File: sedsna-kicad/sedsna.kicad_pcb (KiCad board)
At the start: 2 copper layers, 8.8 x 9.5 mm, 47 parts, among them J1 Conn_01x03, J10 Conn_01x03, J2 Conn_01x03, J3 Servos_Rudder/Elevator, J4 L_Aileron, J5 USB4105-GF-A, J6 R_Aileron, J7 Prop, J8 Antenna, J9 Conn_01x03, U2 ESP32-C3, U4 Magnetometer, U5 IMU, U6 LDL1117S33R

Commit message: pcb layout started
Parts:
- removed BAT1: Conn_01x02, sedsna:CONN_SDA_42002-xxxxx_02_MOL
- removed BR1: Z4DGP406L-HF, TR3_V1:Z4DGP406L-HF_footprint_N
- removed J8: Antenna, sedsna:CONN_142-0701-801
- added AE1: Antenna, TR3_V1:GRADCONN_RFPC-SMA28-F, F.Cu at (125.2, 48.2)
- added J11: BAT1, sedsna:SHDR3W166P0X635_1X3_2032X762X1397P, F.Cu at (122.8, 84.5)
- C15, C17, C18, C23, C24, C3, C4, C5, C6, C7, FB1, R12, R16, R17, R18, R19, R2, R7, R8: moved to B.Cu
- J4, J6, J7: footprint sedsna:CONN_SDA_42002-xxxxx_03_MOL -> sedsna:SHDR3W166P0X635_1X3_2032X762X1397P
- moved L1 123.0 mm to (109.1, 55.2)
- moved U2 122.7 mm to (125.7, 56.6), turned to -45 degrees
- moved C9 122.1 mm to (108.7, 58.5)
- moved C8 122.0 mm to (109.0, 57.0)
- moved XTAL1 114.7 mm to (118.6, 57.0)
- moved B1 113.1 mm to (109.8, 61.0)
- moved C1 111.5 mm to (116.3, 59.7)
- moved C2 111.5 mm to (116.3, 61.7)
- moved C7 108.9 mm to (106.4, 68.2), turned to 180 degrees
- moved C3 108.5 mm to (122.8, 63.8), turned to 180 degrees
- moved U5 106.7 mm to (113.2, 65.8)
- moved FB1 105.3 mm to (122.8, 66.0), turned to 180 degrees
- moved C15 99.9 mm to (113.2, 72.5), turned to 180 degrees
- moved C6 94.3 mm to (105.5, 75.5), turned to 180 degrees
- moved U4 92.8 mm to (106.0, 68.2), turned to 90 degrees
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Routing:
- added copper zone on In2.Cu, net +3.3V
- added copper zone on B.Cu, net Earth
- added copper zone on F.Cu, net Earth
- added copper zone on In1.Cu, net Earth
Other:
- board outline removed
- copper layers 2 -> 4

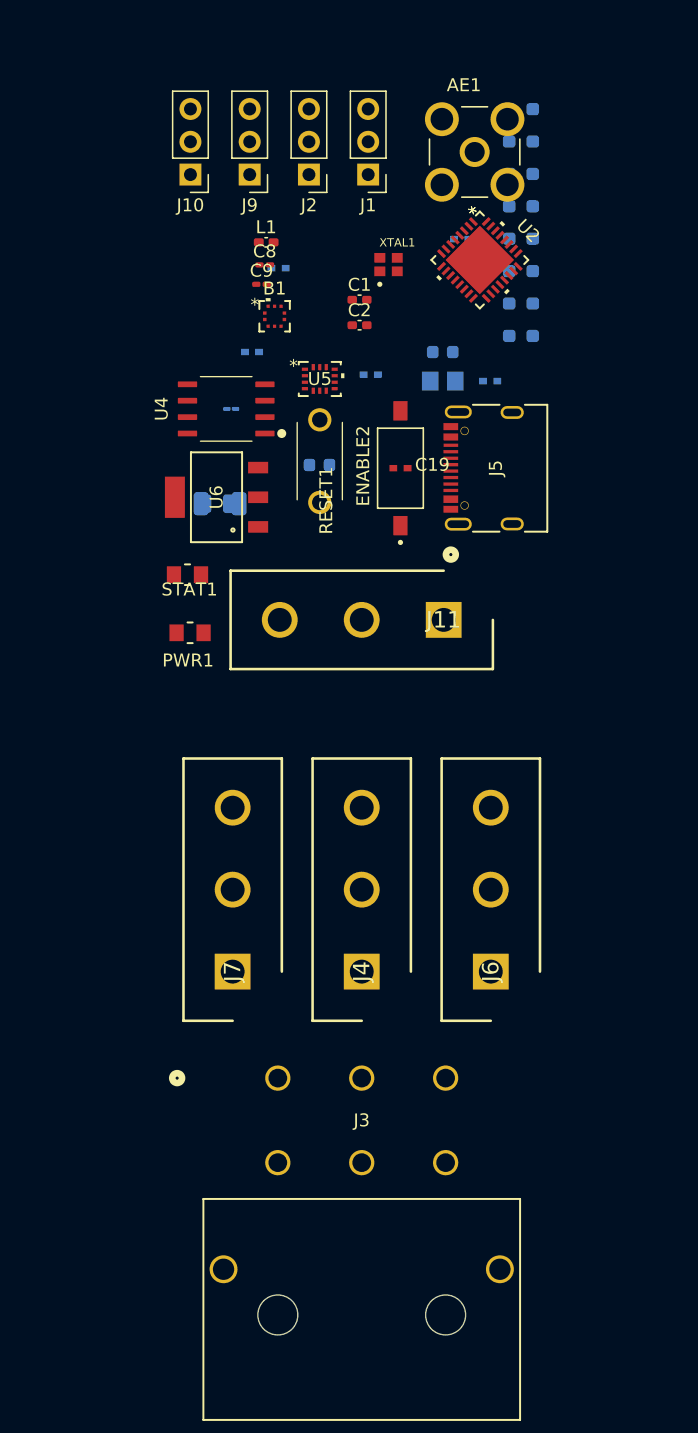
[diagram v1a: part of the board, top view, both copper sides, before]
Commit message: mounting holes added
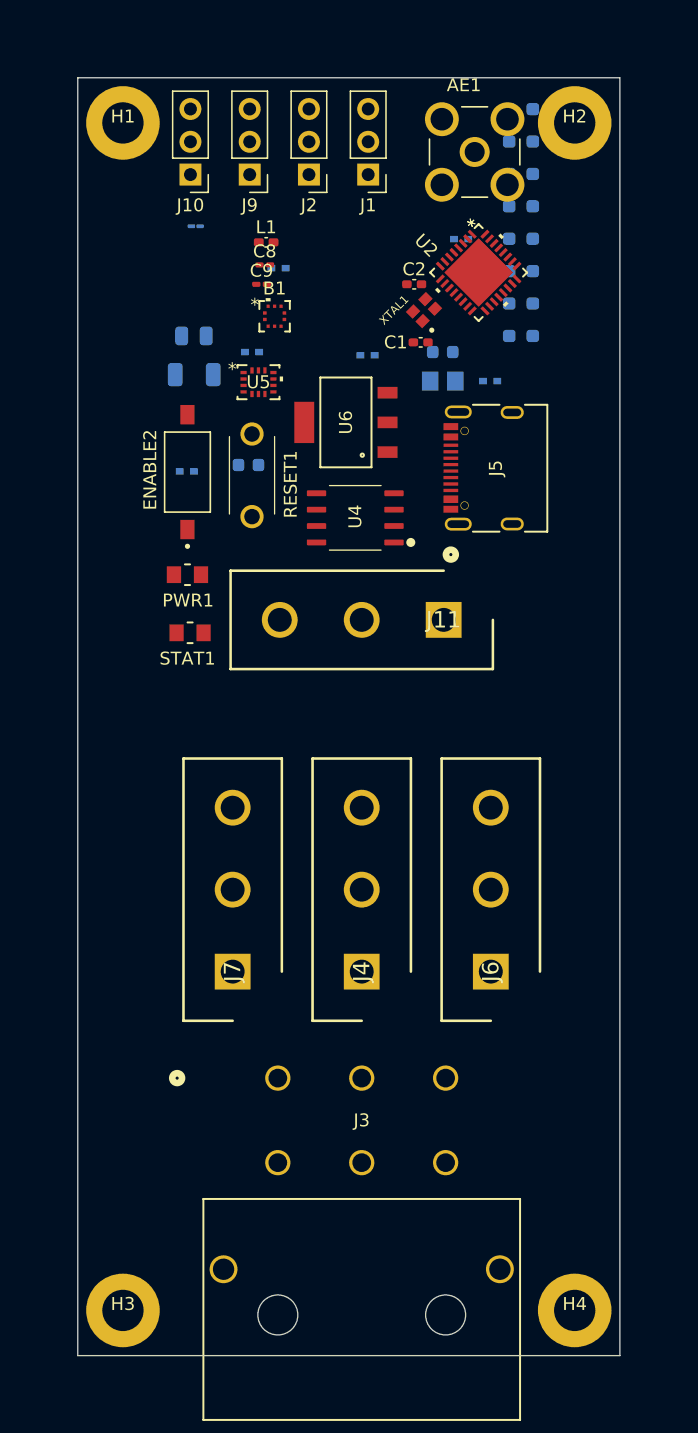
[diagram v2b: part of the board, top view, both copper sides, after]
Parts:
- added H1: MountingHole, sedsna:mounting_hole, F.Cu at (98.0, 46.0)
- added H2: MountingHole, sedsna:mounting_hole, F.Cu at (133.0, 46.0)
- added H3: MountingHole, sedsna:mounting_hole, F.Cu at (98.0, 138.0)
- added H4: MountingHole, sedsna:mounting_hole, F.Cu at (133.0, 138.0)
- C19: moved to B.Cu
- moved C19 16.6 mm to (102.9, 73.0), turned to 180 degrees
- moved ENABLE2 16.5 mm to (103.0, 73.0)
- moved C7 14.4 mm to (103.6, 54.0)
- moved C5 13.1 mm to (103.5, 62.5)
- moved U4 13.1 mm to (116.0, 76.6)
- moved U6 11.6 mm to (115.3, 69.2)
- moved C6 10.2 mm to (103.5, 65.5)
- moved C1 5.77 mm to (121.1, 63.0)
- moved C15 5.50 mm to (107.7, 72.5)
- moved RESET1 5.36 mm to (108.0, 73.3)
- moved C2 5.29 mm to (120.6, 58.5)
- moved U5 4.76 mm to (108.5, 66.1)
- moved XTAL1 4.47 mm to (121.3, 60.5), turned to 45 degrees
- moved C17 1.52 mm to (116.9, 64.0)
- moved U2 0.98 mm to (125.6, 57.6)
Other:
- board outline added: 42 x 99 mm

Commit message: Finished layout
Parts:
- removed ENABLE2: Enable Switch, TR3_V1:SW_DS04-254-2-01BK-SMT
- removed J10, J2, J9: Conn_01x03, Connector_PinHeader_2.54mm:PinHeader_1x03_P2.54mm_Vertical
- C7: footprint Capacitor_SMD:C_01005_0402Metric_Pad0.57x0.30mm_HandSolder -> TR3_V1:CAP_CL05_SAM
- J1: value Conn_01x03 -> ~; footprint Connector_PinHeader_2.54mm:PinHeader_1x03_P2.54mm_Vertical -> sedsna:Conn_04x03
- R2: moved to F.Cu
- moved R7 35.4 mm to (109.0, 76.8), turned to 0 degrees
- moved STAT 28.3 mm to (129.4, 74.7), turned to 90 degrees
- moved PWR 23.4 mm to (125.5, 74.7), turned to 90 degrees
- moved C19 21.8 mm to (122.0, 62.5)
- moved C5 21.6 mm to (118.7, 78.0), turned to 0 degrees
- moved R2 21.5 mm to (126.0, 66.2), turned to -45 degrees
- moved R8 20.4 mm to (111.5, 60.6), turned to 90 degrees
- moved R16 20.0 mm to (125.5, 74.7), turned to 90 degrees
- moved R12 17.6 mm to (113.2, 60.6), turned to 90 degrees
- moved L1 17.6 mm to (125.2, 62.2), turned to 45 degrees
- moved C6 17.5 mm to (120.0, 71.5)
- moved C8 17.4 mm to (126.0, 60.9), turned to 135 degrees
- moved R17 17.2 mm to (129.4, 74.7), turned to 90 degrees
- moved C9 16.5 mm to (124.5, 63.6), turned to -45 degrees
- moved C7 15.6 mm to (108.4, 68.8), turned to -90 degrees
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- renumbered PWR1 to PWR, RESET1 to RESET, STAT1 to STAT
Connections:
- C4 pad 1: +7.4V -> +6.6V
- C5 pad 2: +7.4V -> +6.6V
- FB1 pad 2: +7.4V -> +6.6V
- J11 pad 1: +7.4V -> +6.6V
- J11 pad 3: +7.4V -> unconnected-(J11-Pin_3-Pad3)
- J3 pad 2: +7.4V -> +6.6V
- J3 pad 5: +7.4V -> +6.6V
- J4 pad 2: +7.4V -> +6.6V
- J5 pad A6: /USB_D+ -> Earth
- J5 pad B6: /USB_D+ -> Earth
- J6 pad 2: +7.4V -> +6.6V
- R7 pad 1: Net-(ENABLE2-Pad1) -> +3.3V
- U2 pad 26: /USB_D+ -> Earth
- U2 pad 27: unconnected-(U2-U0RXD-Pad27) -> Earth
- U6 pad 3: +7.4V -> +6.6V
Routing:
- net Net-(AE1-Pad1): track 0.00 -> 3.77 mm
- net /ANT: track 0.00 -> 2.73 mm
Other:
- board size 42 x 99 mm -> 40 x 91 mm
